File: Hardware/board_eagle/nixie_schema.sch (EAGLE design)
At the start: 103 parts, among them J2 RTC_CONSMD, J4 RTC_CONTHT, P1 100k, Q1 BC856B, Q2 IRF740S, T1 PHOTO_TRANS, U2 MC7940N, Y1 ECS-.327-7-34B

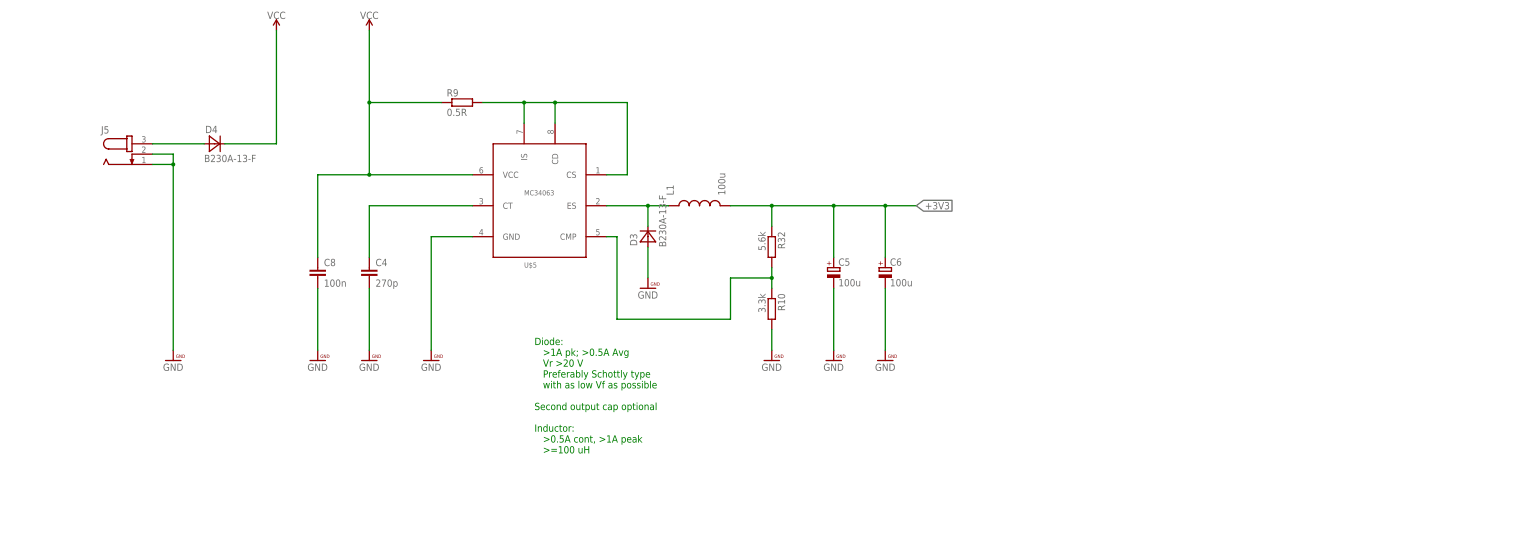
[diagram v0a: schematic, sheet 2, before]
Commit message: Modified both switching PSUs for the new VFD requirements
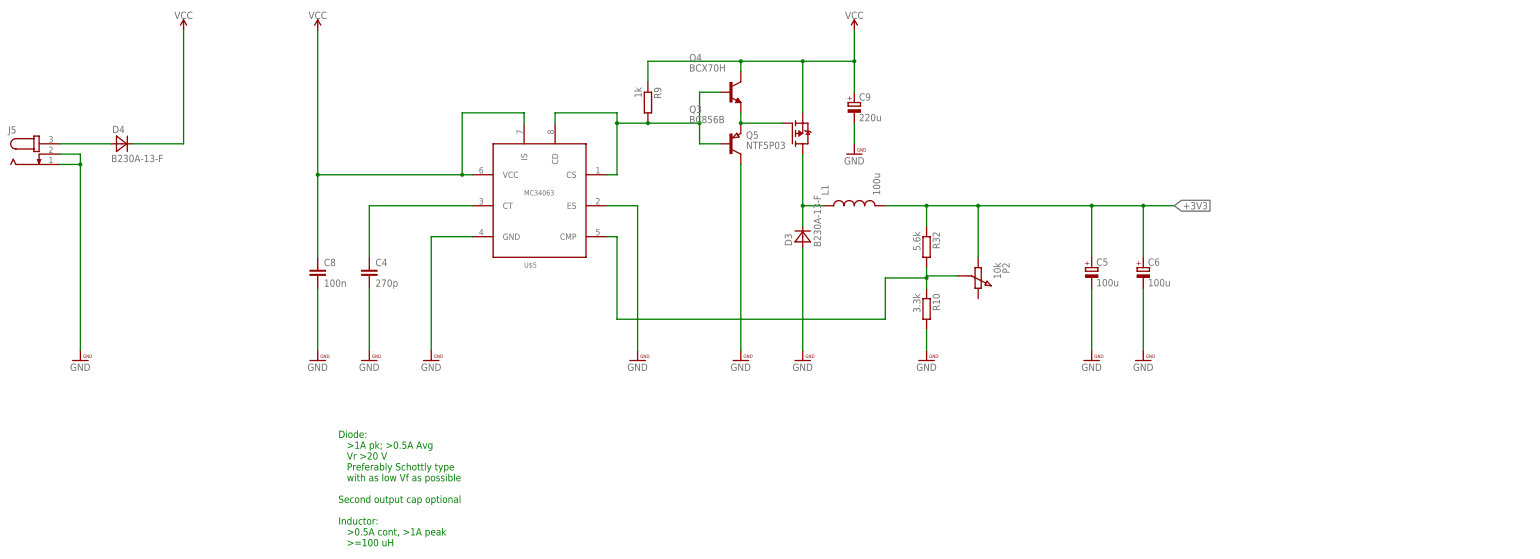
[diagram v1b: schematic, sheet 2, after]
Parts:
- removed Q2: IRF740S, nixe_cmp:IRF740S
- added C9: 220u, rcl:CPOL-EU153CLV-1014
- added P2: 10k, nixe_cmp:UNIVERSAL-POTENTIOMETER_SMD
- added Q3: BC856B, nixe_cmp:BC856B
- added Q4: BCX70H, nixe_cmp:BCX70H
- added Q5: NTF5P03, nixe_cmp:NTF5P03
- added U$36: IPN60R3K4CE_NMOS, nixe_cmp:IPN60R3K4CE_NMOS
- R9: value 0.5R -> 1k; device eagle-ltspice:RR1210 -> resistor:R-EU_R0603
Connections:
- new net N$102: Q3.E, Q4.E, Q5.G
- net +3V3: now also P2.A
- net GND: now also C9.-, Q3.C, U$36.S, U$5.ES; no longer Q2.S
- net N$103: now also P2.WIPER
- net N$13: now also Q5.D; no longer U$5.ES
- net N$5: now also Q3.B, Q4.B; no longer U$5.IS
- net N$95: now also U$36.G; no longer Q2.G
- net VCC: now also C9.+, Q4.C, Q5.S, U$5.IS
- net V_PULSE: now also U$36.D; no longer Q2.D
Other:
- moved on the sheet: C5, C6, D3, D4, J5, L1, R10, R32, R9

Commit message: Modified IN-14 device to accomodate IV-11 VFD
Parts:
- N1, N2, N3, N4, N5, N6: value IN-14_FIXED -> IN-14_IV-11_COMBI; device russian-nixies:IN-14_FIXED -> nixe_cmp:IN-14_IV-11_COMBI
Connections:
- net N$1: now also N2.RHDP(NC); no longer N2.RHDP
- net N$10: now also N1.A(NC); no longer N1.A
- net N$19: now also N2.A(NC); no longer N2.A
- net N$2: now also N1.6(G); no longer N1.6
- net N$21: now also N3.A(NC); no longer N3.A
- net N$23: now also N2.6(G); no longer N2.6
- net N$24: now also N1.9(D); no longer N1.9
- net N$25: now also N1.1(GRID); no longer N1.1
- net N$26: now also N1.2(C); no longer N1.2
- net N$27: now also N1.3(DP); no longer N1.3
- net N$28: now also N1.4(B); no longer N1.4
- net N$29: now also N1.5(A); no longer N1.5
- net N$30: now also N1.RHDP(NC); no longer N1.RHDP
- net N$31: now also N2.7(F); no longer N2.7
- net N$32: now also N2.8(E); no longer N2.8
- net N$33: now also N2.9(D); no longer N2.9
- net N$34: now also N2.0(CAT); no longer N2.0
- net N$35: now also N3.RHDP(NC); no longer N3.RHDP
- net N$36: no longer N3.6
- net N$37: no longer N3.7
- net N$38: now also N2.5(A); no longer N2.5
- net N$39: now also N2.4(B); no longer N2.4
- net N$40: now also N2.3(DP); no longer N2.3
- net N$41: now also N2.2(C); no longer N2.2
- net N$42: now also N2.1(GRID); no longer N2.1
- net N$43: no longer N3.8
- net N$44: no longer N3.9
- net N$45: now also N6.A(NC); no longer N6.A
- net N$46: no longer N3.0
- net N$47: now also N4.RHDP(NC); no longer N4.RHDP
- net N$48: no longer N4.6
- net N$49: no longer N3.5
- net N$50: no longer N3.4
- net N$51: no longer N3.3
- net N$52: no longer N3.2
- net N$53: no longer N3.1
- net N$54: no longer N4.7
- net N$55: no longer N4.8
- net N$56: no longer N4.9
- net N$57: no longer N4.0
- net N$58: now also N5.RHDP(NC); no longer N5.RHDP
- net N$59: no longer N4.5
- net N$6: now also N1.7(F); no longer N1.7
- net N$60: no longer N4.4
- net N$61: no longer N4.3
- net N$62: no longer N4.2
- net N$63: no longer N4.1
- net N$64: no longer N5.6
- net N$65: no longer N5.7
- net N$66: no longer N5.8
- net N$67: no longer N5.9
- net N$68: no longer N5.0
- net N$69: no longer N5.5
- net N$7: now also N1.8(E); no longer N1.8
- net N$70: no longer N5.4
- net N$71: no longer N5.3
- net N$72: no longer N5.2
- net N$73: no longer N5.1
- net N$75: now also N6.RHDP(NC); no longer N6.RHDP
- net N$76: no longer N6.6
- net N$77: no longer N6.7
- net N$78: no longer N6.8
- net N$79: no longer N6.9
- net N$80: no longer N6.5
- net N$81: no longer N6.4
- net N$82: no longer N6.3
- net N$83: no longer N6.2
- net N$84: no longer N6.1
- net N$86: no longer N6.0
- net N$88: now also N4.A(NC); no longer N4.A
- net N$94: now also N1.0(CAT); no longer N1.0
- net N$98: now also N5.A(NC); no longer N5.A

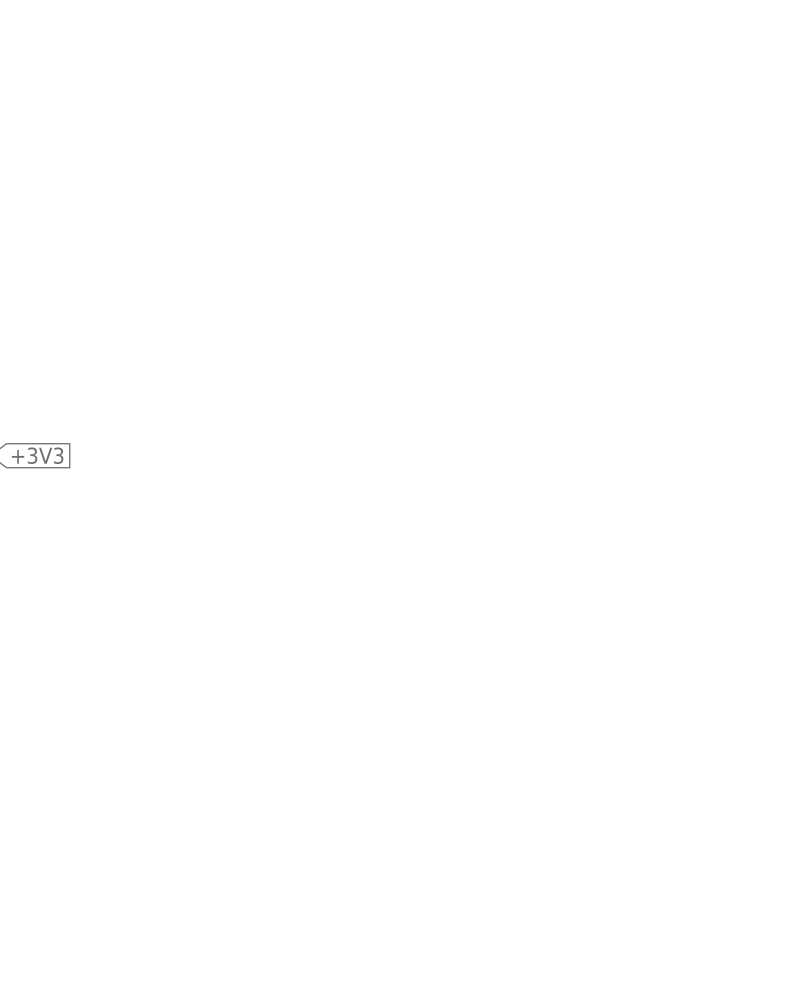
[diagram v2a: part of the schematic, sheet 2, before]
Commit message: Added Eagle libraries for components. New symbols for Solder bridge and cut trace comps
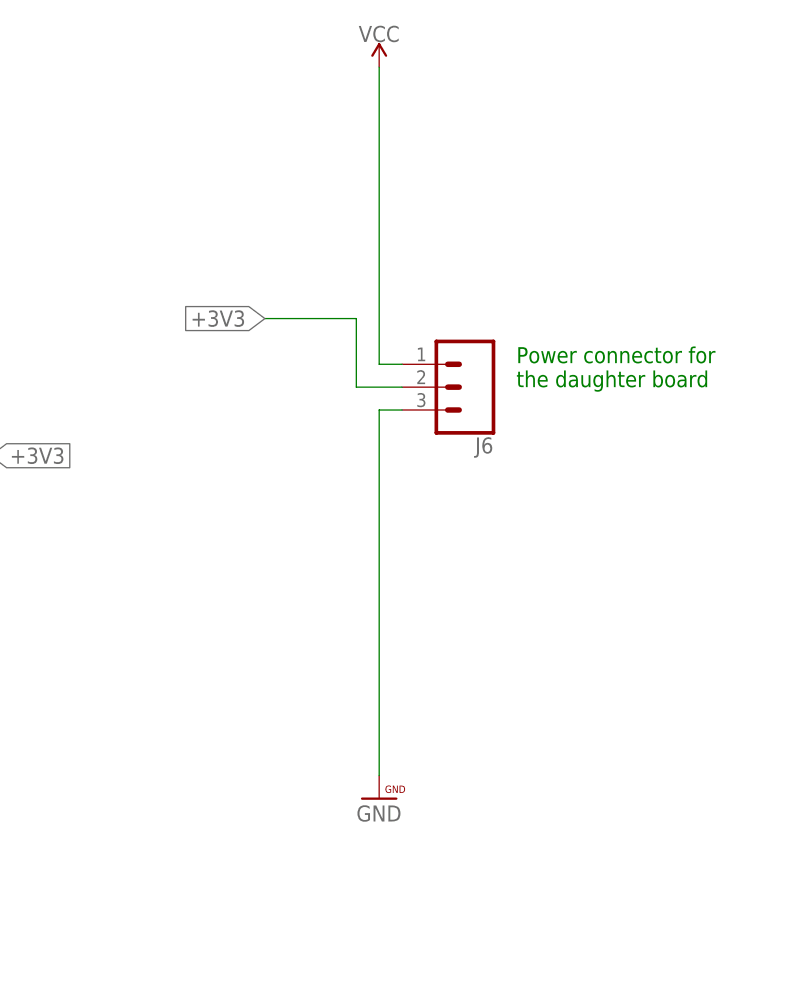
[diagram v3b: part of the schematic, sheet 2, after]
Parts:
- added J6, J7: (no value), SparkFun-Connectors:CONN_03
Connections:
- net +3V3: now also J6.2, J7.2
- net GND: now also J6.3, J7.3
- net VCC: now also J6.1, J7.1
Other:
- note added: "Power connector for the daughter board"
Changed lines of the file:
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@@
 <part name="N5" library="nixe_cmp" deviceset="IN-14_IV-11_COMBI" device=""/>
 <part name="N6" library="nixe_cmp" deviceset="IN-14_IV-11_COMBI" device=""/>
+<part name="J6" library="SparkFun-Connectors" deviceset="CONN_03" device=""/>
+<part name="U$37" library="PatternAgents-Beautify" deviceset="GND" device=""/>
+<part name="SUPPLY10" library="SparkFun-PowerSymbols" deviceset="VCC" device=""/>
+<part name="J7" library="SparkFun-Connectors" deviceset="CONN_03" device=""/>
+<part name="U$38" library="PatternAgents-Beautify" deviceset="GND" device=""/>
+<part name="SUPPLY11" library="SparkFun-PowerSymbols" deviceset="VCC" device=""/>
 </parts>
 <sheets>
@@
    &gt;0.5A cont, &gt;1A peak
    &gt;=100 uH</text>
+<text x="269.24" y="76.2" size="1.778" layer="91">Power connector for
+the daughter board</text>
 </plain>
 <instances>
@@
 <instance part="Q5" gate="G$1" x="116.84" y="86.36" rot="MR180"/>
 <instance part="U$35" gate="G$1" x="104.14" y="33.02"/>
+<instance part="J6" gate="J$1" x="264.16" y="76.2" rot="R180"/>
+<instance part="U$37" gate="G$1" x="254" y="33.02"/>
+<instance part="SUPPLY10" gate="G$1" x="254" y="111.76"/>
 </instances>
 <busses>
@@
 <junction x="162.56" y="68.58"/>
 </segment>
+<segment>
+<pinref part="J6" gate="J$1" pin="2"/>
+<wire x1="256.54" y1="76.2" x2="251.46" y2="76.2" width="0.1524" layer="91"/>
+<wire x1="251.46" y1="76.2" x2="251.46" y2="83.82" width="0.1524" layer="91"/>
+<wire x1="251.46" y1="83.82" x2="241.3" y2="83.82" width="0.1524" layer="91"/>
+<label x="241.3" y="83.82" size="1.778" layer="95" rot="R180" xref="yes"/>
+</segment>
 </net>
 <net name="GND" class="0">
@@
 <pinref part="Q3" gate="Q$1" pin="C"/>
 <wire x1="104.14" y1="33.02" x2="104.14" y2="78.74" width="0.1524" layer="91"/>
+</segment>
+<segment>
+<pinref part="U$37" gate="G$1" pin="GND"/>
+<wire x1="254" y1="33.02" x2="254" y2="73.66" width="0.1524" layer="91"/>
+<pinref part="J6" gate="J$1" pin="3"/>
+<wire x1="254" y1="73.66" x2="256.54" y2="73.66" width="0.1524" layer="91"/>
 </segment>
 </net>
@@
 <junction x="119.38" y="104.14"/>
 <junction x="132.08" y="104.14"/>
+</segment>
+<segment>
+<pinref part="SUPPLY10" gate="G$1" pin="VCC"/>
+<wire x1="254" y1="111.76" x2="254" y2="78.74" width="0.1524" layer="91"/>
+<pinref part="J6" gate="J$1" pin="1"/>
+<wire x1="254" y1="78.74" x2="256.54" y2="78.74" width="0.1524" layer="91"/>
 </segment>
 </net>
@@
 <instance part="N5" gate="G$1" x="304.8" y="12.7" rot="R270"/>
 <instance part="N6" gate="G$1" x="378.46" y="12.7" rot="R270"/>
+<instance part="J7" gate="J$1" x="-48.26" y="30.48" rot="R180"/>
+<instance part="U$38" gate="G$1" x="-58.42" y="-12.7"/>
+<instance part="SUPPLY11" gate="G$1" x="-58.42" y="66.04"/>
 </instances>
 <busses>
@@
 </segment>
 </net>
+<net name="+3V3" class="3">
+<segment>
+<wire x1="-55.88" y1="30.48" x2="-60.96" y2="30.48" width="0.1524" layer="91"/>
+<wire x1="-60.96" y1="30.48" x2="-60.96" y2="38.1" width="0.1524" layer="91"/>
+<wire x1="-60.96" y1="38.1" x2="-71.12" y2="38.1" width="0.1524" layer="91"/>
+<label x="-71.12" y="38.1" size="1.778" layer="95" rot="R180" xref="yes"/>
+<pinref part="J7" gate="J$1" pin="2"/>
+</segment>
+</net>
+<net name="GND" class="0">
+<segment>
+<pinref part="U$38" gate="G$1" pin="GND"/>
+<wire x1="-58.42" y1="-12.7" x2="-58.42" y2="27.94" width="0.1524" layer="91"/>
+<wire x1="-58.42" y1="27.94" x2="-55.88" y2="27.94" width="0.1524" layer="91"/>
+<pinref part="J7" gate="J$1" pin="3"/>
+</segment>
+</net>
+<net name="VCC" class="1">
+<segment>
+<pinref part="SUPPLY11" gate="G$1" pin="VCC"/>
+<wire x1="-58.42" y1="66.04" x2="-58.42" y2="33.02" width="0.1524" layer="91"/>
+<wire x1="-58.42" y1="33.02" x2="-55.88" y2="33.02" width="0.1524" layer="91"/>
+<pinref part="J7" gate="J$1" pin="1"/>
+</segment>
+</net>

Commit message: Hopefully fixed compined tube footprint for good
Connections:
- net N$10: now also N1.A(A); no longer N1.A(NC)
- net N$19: now also N2.A(A); no longer N2.A(NC)
- net N$2: now also N1.6(CAT); no longer N1.6(G)
- net N$21: now also N3.A(A); no longer N3.A(NC)
- net N$23: now also N2.6(CAT); no longer N2.6(G)
- net N$24: now also N1.9(DP); no longer N1.9(D)
- net N$25: now also N1.1(F); no longer N1.1(GRID)
- net N$26: now also N1.2(E); no longer N1.2(C)
- net N$27: now also N1.3(D); no longer N1.3(DP)
- net N$28: now also N1.4(CAT); no longer N1.4(B)
- net N$29: now also N1.5(NC); no longer N1.5(A)
- net N$31: now also N2.7(GRID); no longer N2.7(F)
- net N$32: now also N2.8(C); no longer N2.8(E)
- net N$33: now also N2.9(DP); no longer N2.9(D)
- net N$34: now also N2.0(B); no longer N2.0(CAT)
- net N$36: now also N3.6(CAT)
- net N$37: now also N3.7(GRID)
- net N$38: now also N2.5(NC); no longer N2.5(A)
- net N$39: now also N2.4(CAT); no longer N2.4(B)
- net N$40: now also N2.3(D); no longer N2.3(DP)
- net N$41: now also N2.2(E); no longer N2.2(C)
- net N$42: now also N2.1(F); no longer N2.1(GRID)
- net N$43: now also N3.8(C)
- net N$44: now also N3.9(DP)
- net N$45: now also N6.A(A); no longer N6.A(NC)
- net N$46: now also N3.0(B)
- net N$48: now also N4.6(CAT)
- net N$49: now also N3.5(NC)
- net N$50: now also N3.4(CAT)
- net N$51: now also N3.3(D)
- net N$52: now also N3.2(E)
- net N$53: now also N3.1(F)
- net N$54: now also N4.7(GRID)
- net N$55: now also N4.8(C)
- net N$56: now also N4.9(DP)
- net N$57: now also N4.0(B)
- net N$59: now also N4.5(NC)
- net N$6: now also N1.7(GRID); no longer N1.7(F)
- net N$60: now also N4.4(CAT)
- net N$61: now also N4.3(D)
- net N$62: now also N4.2(E)
- net N$63: now also N4.1(F)
- net N$64: now also N5.6(CAT)
- net N$65: now also N5.7(GRID)
- net N$66: now also N5.8(C)
- net N$67: now also N5.9(DP)
- net N$68: now also N5.0(B)
- net N$69: now also N5.5(NC)
- net N$7: now also N1.8(C); no longer N1.8(E)
- net N$70: now also N5.4(CAT)
- net N$71: now also N5.3(D)
- net N$72: now also N5.2(E)
- net N$73: now also N5.1(F)
- net N$76: now also N6.6(CAT)
- net N$77: now also N6.7(GRID)
- net N$78: now also N6.8(C)
- net N$79: now also N6.9(DP)
- net N$80: now also N6.5(NC)
- net N$81: now also N6.4(CAT)
- net N$82: now also N6.3(D)
- net N$83: now also N6.2(E)
- net N$84: now also N6.1(F)
- net N$86: now also N6.0(B)
- net N$88: now also N4.A(A); no longer N4.A(NC)
- net N$94: now also N1.0(B); no longer N1.0(CAT)
- net N$98: now also N5.A(A); no longer N5.A(NC)
